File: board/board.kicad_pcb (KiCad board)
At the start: 2 copper layers, 21 x 13 mm, 6 parts, among them J1 001_I2C, J2 001_I2C, U1 LPS25HB

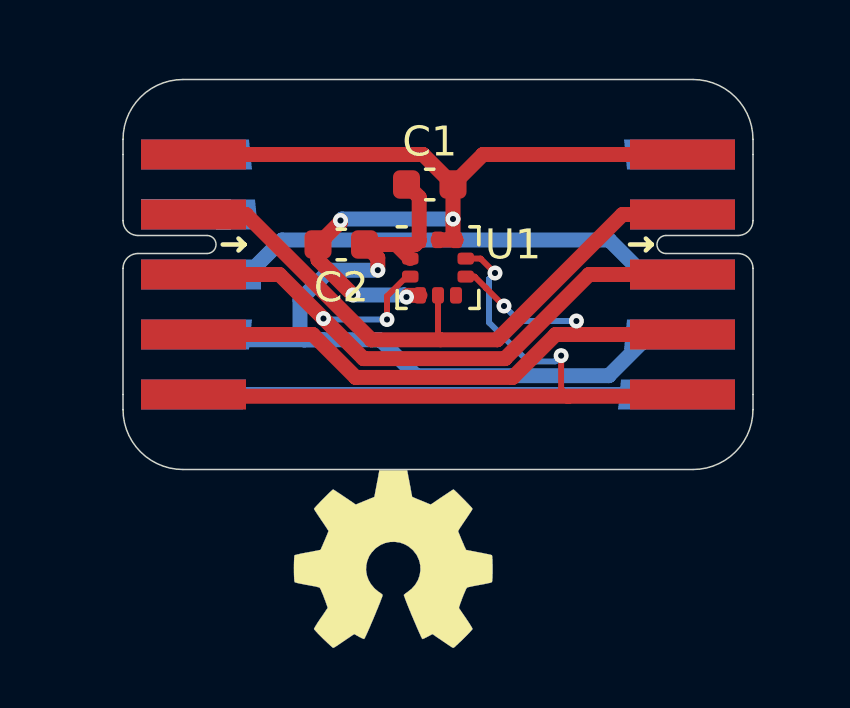
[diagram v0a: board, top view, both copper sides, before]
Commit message: added ground plane
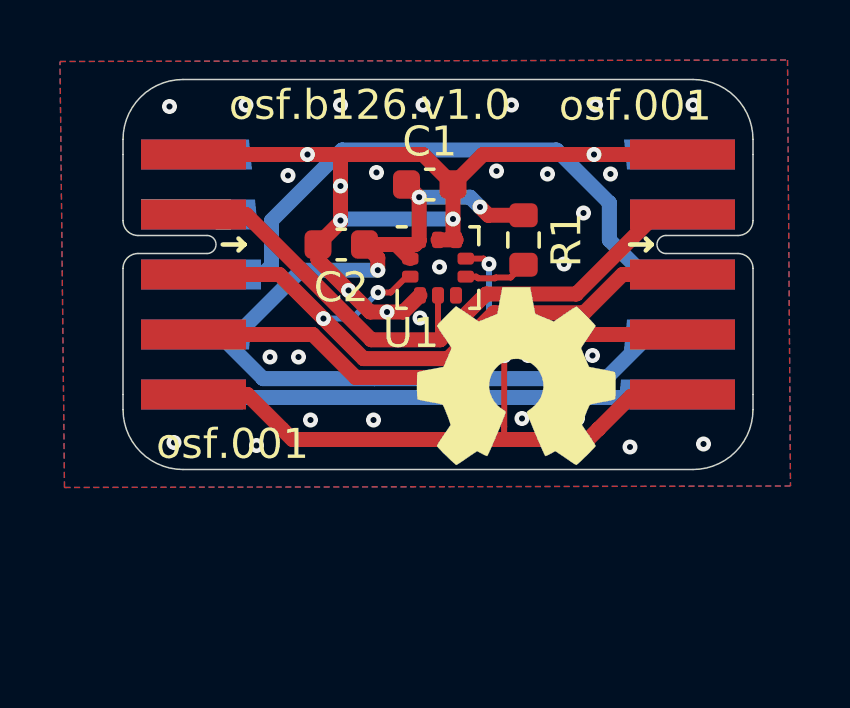
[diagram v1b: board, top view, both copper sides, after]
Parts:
- added R1: 0R, Resistor_SMD:R_0603_1608Metric, F.Cu at (153.3, 95.3)
- moved LOGO1 7.35 mm to (153.1, 99.9)
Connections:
- J1 pad 4: /pressure/~{CS} -> Net-(J1-Pad4)
- J2 pad 4: /pressure/~{CS} -> Net-(J1-Pad4)
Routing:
- net /pressure/~{CS}: track 22.3 -> 2.14 mm, vias 2 -> 0
- net Net-(J1-Pad4): track 0.00 -> 17.5 mm
- net /pressure/VDD: track 28.0 -> 33.0 mm, vias 1 -> 3
- net Net-(J1-Pad8): track 17.0 -> 21.1 mm
- net GND: track 28.9 -> 31.6 mm, vias 4 -> 38
- net /pressure/INT: track 23.7 -> 24.5 mm
- added copper zone on B.Cu, net GND
- added copper zone on F.Cu, net GND
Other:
- board text added: "osf.001"
- board text added: "osf.b126.v1.0"
